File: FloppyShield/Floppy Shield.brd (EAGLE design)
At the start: 68.6 x 53.3 mm, 13 parts

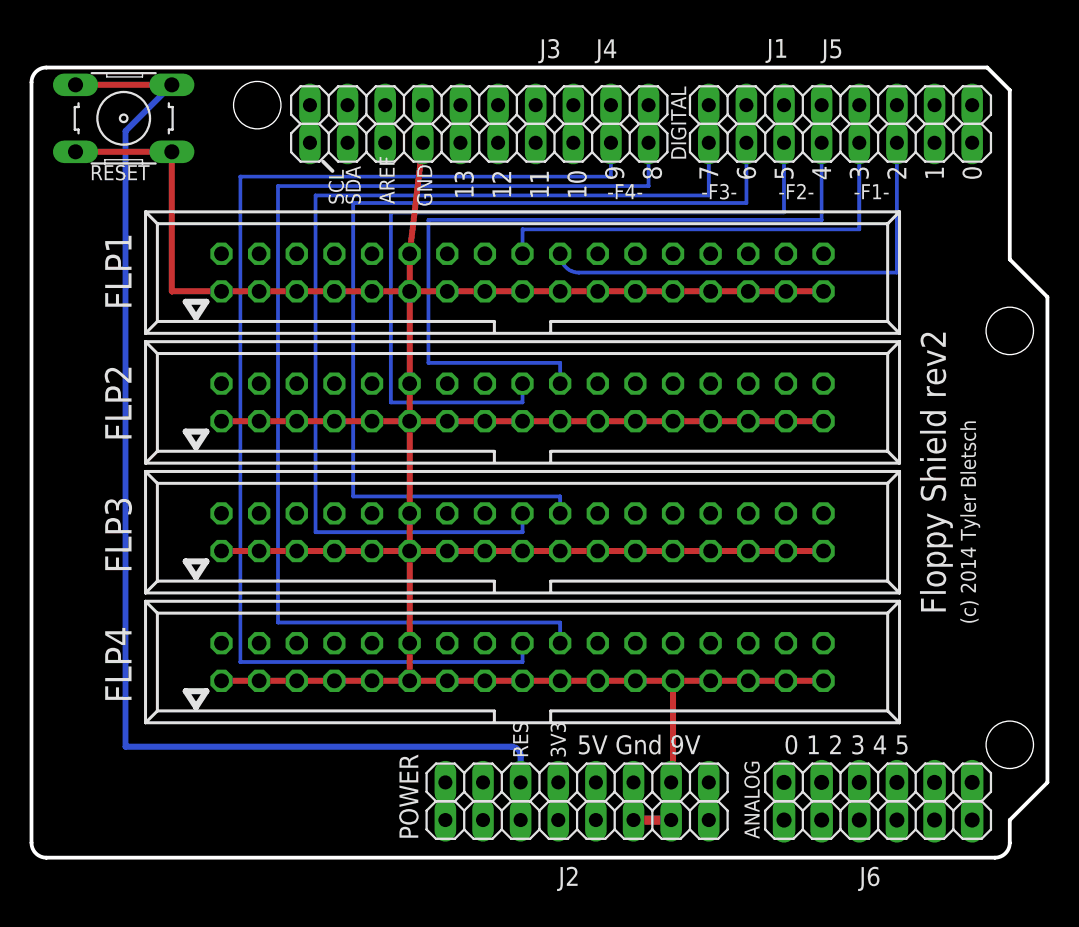
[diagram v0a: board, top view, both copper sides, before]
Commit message: Shield now works with "crossover" floppy cables  (grounded DRIVE A SELECT)
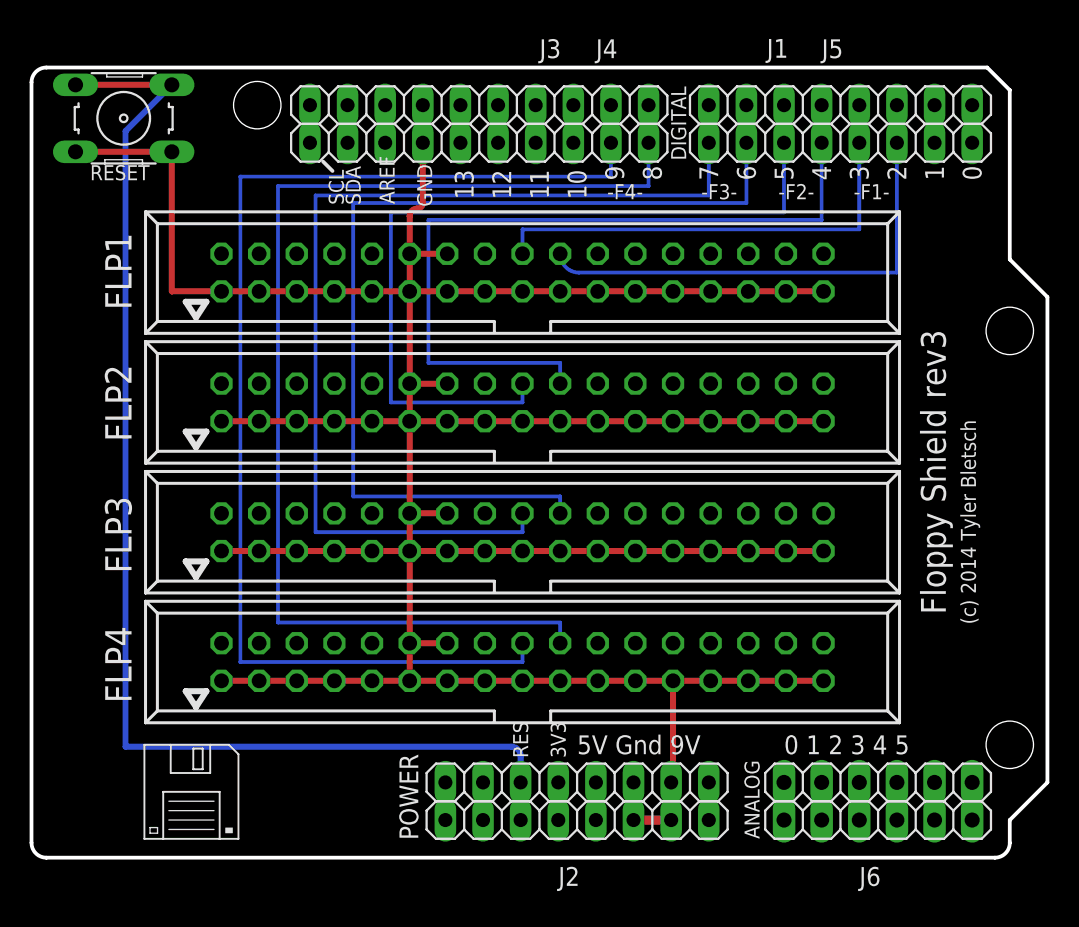
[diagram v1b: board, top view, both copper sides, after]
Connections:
- net GND: now also FLP1.14, FLP2.14, FLP3.14, FLP4.14
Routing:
- net GND: track 235.4 -> 245.8 mm
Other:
- board text added: "Floppy Shield rev3"
- board text removed: "Floppy Shield rev2"
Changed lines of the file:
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@@
 <setting verticaltext="up"/>
 </settings>
-<grid distance="5" unitdist="mil" unit="mil" style="lines" multiple="1" display="yes" altdistance="25" altunitdist="mil" altunit="mil"/>
+<grid distance="50" unitdist="mil" unit="mil" style="lines" multiple="1" display="yes" altdistance="5" altunitdist="mil" altunit="mil"/>
 <layers>
 <layer number="1" name="Top" color="4" fill="1" visible="yes" active="yes"/>
@@
 <text x="36.83" y="6.985" size="1.27" layer="25" font="vector" ratio="12">5V Gnd 9V</text>
 <text x="50.8" y="6.985" size="1.27" layer="25" font="vector" ratio="12">0 1 2 3 4 5</text>
-<text x="61.722" y="26.035" size="1.6764" layer="21" font="vector" ratio="12" rot="R90" align="bottom-center">Floppy Shield rev2</text>
+<text x="61.722" y="26.035" size="1.6764" layer="21" font="vector" ratio="12" rot="R90" align="bottom-center">Floppy Shield rev3</text>
 <text x="29.845" y="44.45" size="1.27" layer="21" font="vector" ratio="12" rot="R90">13</text>
 <text x="32.385" y="44.45" size="1.27" layer="21" font="vector" ratio="12" rot="R90">12</text>
@@
 <dimension x1="0.127" y1="-6.731" x2="68.707" y2="-6.731" x3="34.417" y3="-12.319" textsize="1.016" textratio="10" layer="48"/>
 <dimension x1="0" y1="52.34" x2="0.127" y2="-0.254" x3="-9.33383125" y3="26.02030625" textsize="1.016" textratio="10" layer="48"/>
+<wire x1="7.62" y1="7.62" x2="7.62" y2="1.27" width="0.127" layer="25"/>
+<wire x1="7.62" y1="1.27" x2="8.89" y2="1.27" width="0.127" layer="25"/>
+<wire x1="8.89" y1="1.27" x2="12.7" y2="1.27" width="0.127" layer="25"/>
+<wire x1="12.7" y1="1.27" x2="13.97" y2="1.27" width="0.127" layer="25"/>
+<wire x1="13.97" y1="1.27" x2="13.97" y2="6.985" width="0.127" layer="25"/>
+<wire x1="13.97" y1="6.985" x2="13.335" y2="7.62" width="0.127" layer="25"/>
+<wire x1="13.335" y1="7.62" x2="12.065" y2="7.62" width="0.127" layer="25"/>
+<wire x1="12.065" y1="7.62" x2="9.398" y2="7.62" width="0.127" layer="25"/>
+<wire x1="9.398" y1="7.62" x2="7.62" y2="7.62" width="0.127" layer="25"/>
+<wire x1="9.398" y1="7.62" x2="9.398" y2="5.715" width="0.127" layer="25"/>
+<wire x1="9.398" y1="5.715" x2="12.065" y2="5.715" width="0.127" layer="25"/>
+<wire x1="12.065" y1="5.715" x2="12.065" y2="7.62" width="0.127" layer="25"/>
+<wire x1="8.89" y1="1.27" x2="8.89" y2="4.445" width="0.127" layer="25"/>
+<wire x1="8.89" y1="4.445" x2="12.7" y2="4.445" width="0.127" layer="25"/>
+<wire x1="12.7" y1="4.445" x2="12.7" y2="1.27" width="0.127" layer="25"/>
+<wire x1="10.922" y1="7.366" x2="11.557" y2="7.366" width="0.127" layer="25"/>
+<wire x1="11.557" y1="7.366" x2="11.557" y2="5.969" width="0.127" layer="25"/>
+<wire x1="11.557" y1="5.969" x2="10.922" y2="5.969" width="0.127" layer="25"/>
+<wire x1="10.922" y1="5.969" x2="10.922" y2="7.366" width="0.127" layer="25"/>
+<wire x1="9.271" y1="3.81" x2="12.319" y2="3.81" width="0.0762" layer="25"/>
+<wire x1="12.319" y1="3.175" x2="9.271" y2="3.175" width="0.0762" layer="25"/>
+<wire x1="9.271" y1="2.54" x2="12.319" y2="2.54" width="0.0762" layer="25"/>
+<wire x1="12.319" y1="1.905" x2="9.271" y2="1.905" width="0.0762" layer="25"/>
+<rectangle x1="13.081" y1="1.651" x2="13.589" y2="2.032" layer="25"/>
+<wire x1="8.001" y1="2.032" x2="8.509" y2="2.032" width="0.0762" layer="25"/>
+<wire x1="8.509" y1="2.032" x2="8.509" y2="1.651" width="0.0762" layer="25"/>
+<wire x1="8.509" y1="1.651" x2="8.001" y2="1.651" width="0.0762" layer="25"/>
+<wire x1="8.001" y1="1.651" x2="8.001" y2="2.032" width="0.0762" layer="25"/>
 </plain>
 <attributes>
@@
 <contactref element="J3" pad="7"/>
 <contactref element="J4" pad="7"/>
-<wire x1="26.416" y1="48.26" x2="25.527" y2="40.767" width="0.4064" layer="1"/>
 <wire x1="25.527" y1="40.767" x2="25.527" y2="38.227" width="0.4064" layer="1"/>
 <wire x1="25.527" y1="38.227" x2="25.527" y2="32.004" width="0.4064" layer="1"/>
@@
 <wire x1="43.18" y1="2.54" x2="40.64" y2="2.54" width="0.6096" layer="1"/>
 <wire x1="26.416" y1="48.26" x2="26.416" y2="50.8" width="0.6096" layer="1"/>
+<contactref element="FLP2" pad="14"/>
+<contactref element="FLP1" pad="14"/>
+<contactref element="FLP3" pad="14"/>
+<contactref element="FLP4" pad="14"/>
+<wire x1="28.067" y1="40.767" x2="25.527" y2="40.767" width="0.4064" layer="1"/>
+<wire x1="28.067" y1="32.004" x2="25.527" y2="32.004" width="0.4064" layer="1"/>
+<wire x1="28.067" y1="23.241" x2="25.527" y2="23.241" width="0.4064" layer="1"/>
+<wire x1="28.067" y1="14.478" x2="25.527" y2="14.478" width="0.4064" layer="1"/>
+<wire x1="26.416" y1="48.26" x2="26.416" y2="44.196" width="0.4064" layer="1"/>
+<wire x1="26.416" y1="44.196" x2="26.035" y2="43.815" width="0.4064" layer="1" curve="-90"/>
+<wire x1="26.035" y1="43.815" x2="25.527" y2="43.307" width="0.4064" layer="1" curve="90"/>
+<wire x1="25.527" y1="43.307" x2="25.527" y2="40.767" width="0.4064" layer="1"/>
 </signal>
 <signal name="N$31">
